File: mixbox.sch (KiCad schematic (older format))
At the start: 20 parts, among them J1 Conn_01x05_Male, J2 Conn_01x06_Male, SW1 SW_Push, SW2 SW_Push, SW3 SW_Push, SW4 SW_Push, SW5 SW_Push, SW6 SW_Push, SW7 SW_Push, SW8 SW_Push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

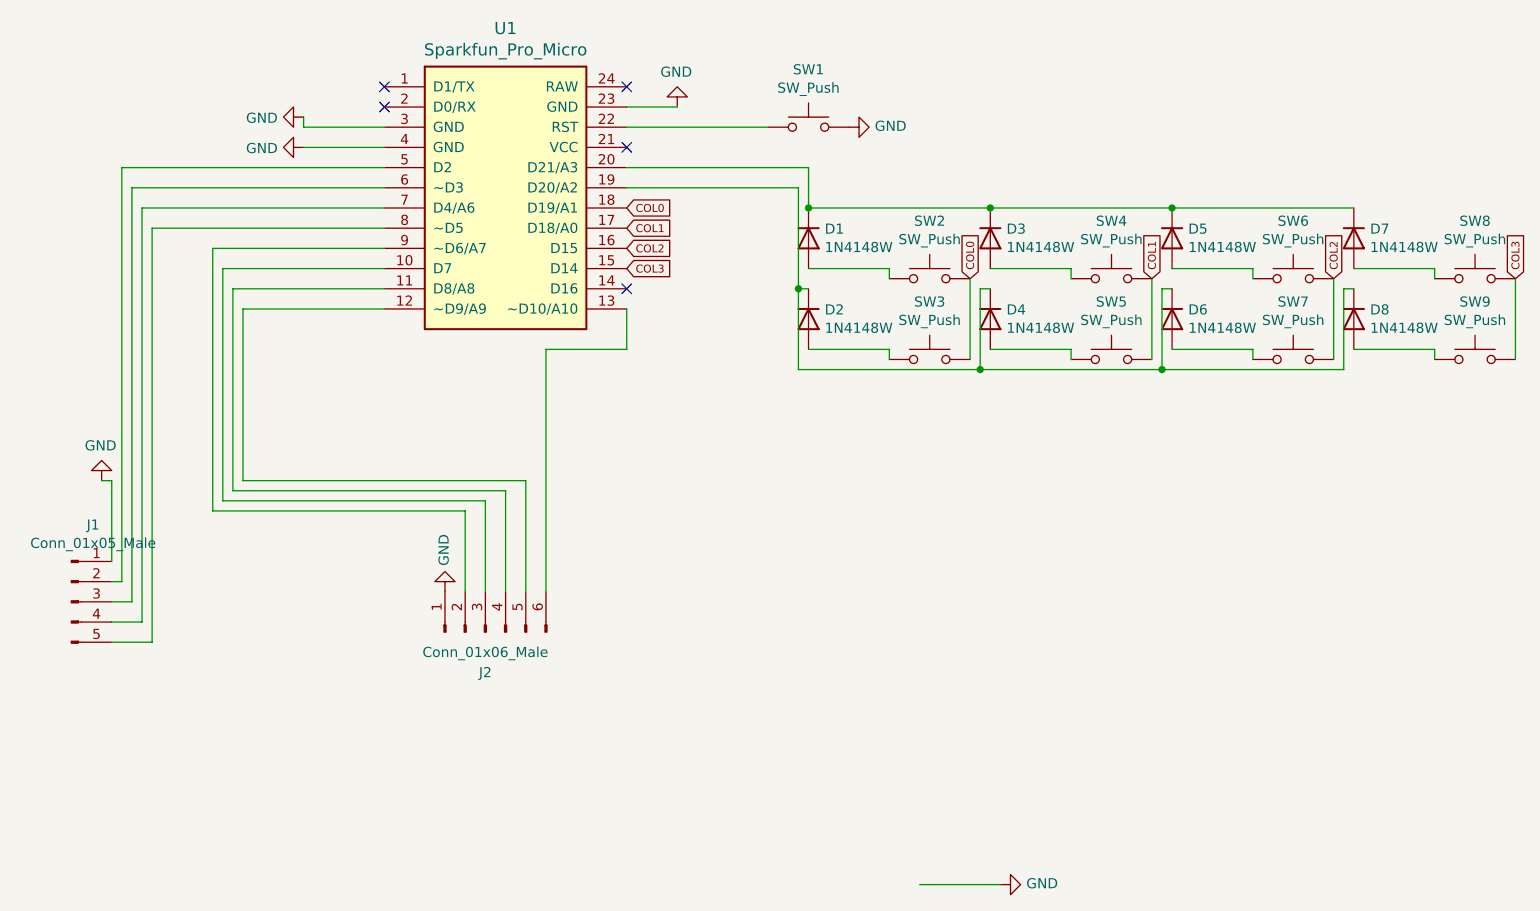
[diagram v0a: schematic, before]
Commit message: Updates schematic for 2 extra rows and columns from direct pin from the J1 and J2 connectors
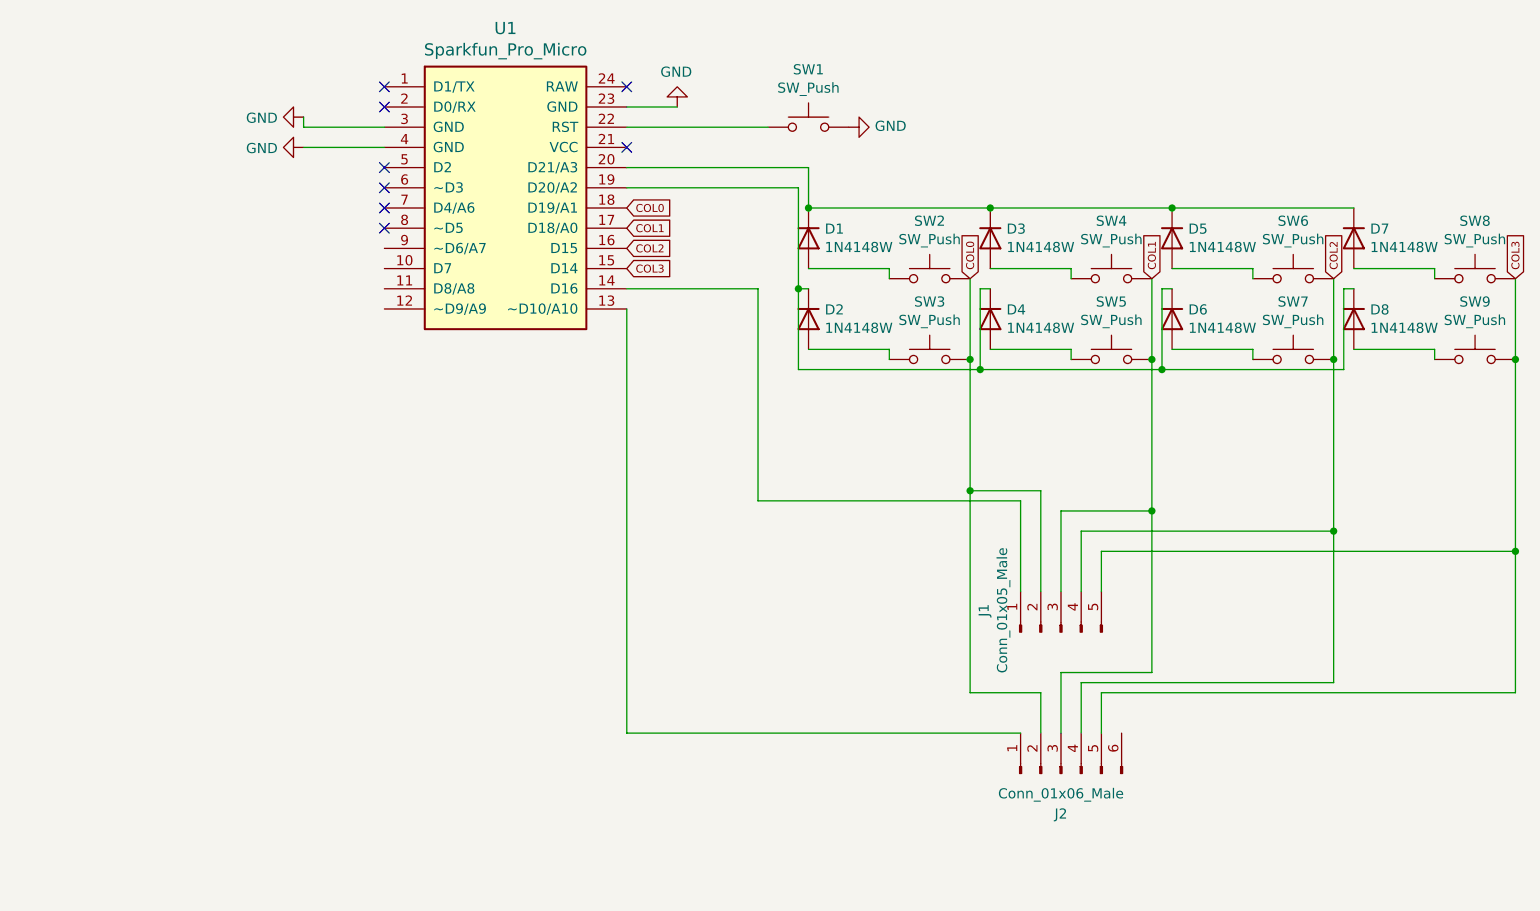
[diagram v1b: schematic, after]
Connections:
- net COL0: now also J1.2 (Pin_2), J2.2 (Pin_2)
- net COL1: now also J1.3 (Pin_3), J2.3 (Pin_3)
- net COL2: now also J1.4 (Pin_4), J2.4 (Pin_4)
- net COL3: now also J1.5 (Pin_5), J2.5 (Pin_5)
- net GND: no longer J1.1 (Pin_1), J2.1 (Pin_1)
- net at U1.9 (~~D6/A7): no longer J2.2 (Pin_2)
- net at U1.10 (D7): no longer J2.3 (Pin_3)
- net at U1.11 (D8/A8): no longer J2.4 (Pin_4)
- net at U1.12 (~~D9/A9): no longer J2.5 (Pin_5)
- net at U1.13 (~~D10/A10): now also J2.1 (Pin_1); no longer J2.6 (Pin_6)
- net at U1.14 (D16): now also J1.1 (Pin_1)
- net at U1.5 (D2): no longer J1.2 (Pin_2)
- net at U1.6 (~~D3): no longer J1.3 (Pin_3)
- net at U1.7 (D4/A6): no longer J1.4 (Pin_4)
- net at U1.8 (~~D5): no longer J1.5 (Pin_5)
- no-connect marks 5 -> 8
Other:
- moved on the sheet: J1, J2
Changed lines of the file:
@@
 $EndComp
-$Comp
-L power:GND #PWR03
-U 1 1 61D25670
-P 5300 5000
-F 0 "#PWR03" H 5300 4750 50  0001 C CNN
-F 1 "GND" V 5305 4872 50  0000 R CNN
-F 2 "" H 5300 5000 50  0001 C CNN
-F 3 "" H 5300 5000 50  0001 C CNN
-	1    5300 5000
-	0    -1   -1   0
-$EndComp
-Wire Wire Line
-	4900 5000 5300 5000
 $Comp
 L Switch:SW_Push SW1
@@
 $EndComp
 Wire Wire Line
-	4350 1950 4750 1950
-Wire Wire Line
 	4750 1950 4750 2000
 Wire Wire Line
@@
 	5200 2450 4300 2450
 Wire Wire Line
-	4300 2450 4300 2050
-Wire Wire Line
 	4300 2050 4350 2050
 Connection ~ 5200 2450
@@
 	4300 1550 3450 1550
 Connection ~ 4300 2050
-$Comp
-L Connector:Conn_01x05_Male J1
-U 1 1 61D20DF3
-P 700 3600
-F 0 "J1" H 808 3981 50  0000 C CNN
-F 1 "Conn_01x05_Male" H 808 3890 50  0000 C CNN
-F 2 "Connector_JST:JST_PH_S5B-PH-K_1x05_P2.00mm_Horizontal" H 700 3600 50  0001 C CNN
-F 3 "~" H 700 3600 50  0001 C CNN
-	1    700  3600
-	1    0    0    -1
-$EndComp
-Wire Wire Line
-	900  3500 950  3500
-Wire Wire Line
-	900  3600 1000 3600
-Wire Wire Line
-	900  3700 1050 3700
-$Comp
-L power:GND #PWR01
-U 1 1 61DB55A5
-P 850 3000
-F 0 "#PWR01" H 850 2750 50  0001 C CNN
-F 1 "GND" H 855 2827 50  0000 C CNN
-F 2 "" H 850 3000 50  0001 C CNN
-F 3 "" H 850 3000 50  0001 C CNN
-	1    850  3000
-	-1   0    0    1
-$EndComp
 $Comp
 L power:GND #PWR0101
@@
 Text GLabel 3450 1950 2    39   Input ~ 0
 COL3
-NoConn ~ 3450 2050
 NoConn ~ 3450 1350
 NoConn ~ 3450 1050
@@
 Wire Wire Line
 	1850 1250 1850 1200
-Wire Wire Line
-	900  3400 900  3000
-Wire Wire Line
-	900  3000 850  3000
-Wire Wire Line
-	950  1450 2250 1450
-Wire Wire Line
-	950  1450 950  3500
-Wire Wire Line
-	1000 1550 2250 1550
-Wire Wire Line
-	1000 1550 1000 3600
-Wire Wire Line
-	1050 1650 2250 1650
-Wire Wire Line
-	1050 1650 1050 3700
-Wire Wire Line
-	900  3800 1100 3800
-Wire Wire Line
-	1100 3800 1100 1750
-Wire Wire Line
-	1100 1750 2250 1750
 $Comp
 L Connector:Conn_01x06_Male J2
 U 1 1 61CFB837
-P 2750 3750
-F 0 "J2" V 2550 3750 50  0000 C CNN
-F 1 "Conn_01x06_Male" V 2650 3750 50  0000 C CNN
-F 2 "Connector_JST:JST_PH_S6B-PH-K_1x06_P2.00mm_Horizontal" H 2750 3750 50  0001 C CNN
-F 3 "~" H 2750 3750 50  0001 C CNN
-	1    2750 3750
+P 5600 4450
+F 0 "J2" V 5400 4450 50  0000 C CNN
+F 1 "Conn_01x06_Male" V 5500 4450 50  0000 C CNN
+F 2 "Connector_JST:JST_PH_S6B-PH-K_1x06_P2.00mm_Horizontal" H 5600 4450 50  0001 C CNN
+F 3 "~" H 5600 4450 50  0001 C CNN
+	1    5600 4450
 	0    -1   -1   0
 $EndComp
-$Comp
-L power:GND #PWR0104
-U 1 1 61D007FD
-P 2550 3550
-F 0 "#PWR0104" H 2550 3300 50  0001 C CNN
-F 1 "GND" V 2555 3422 50  0000 R CNN
-F 2 "" H 2550 3550 50  0001 C CNN
-F 3 "" H 2550 3550 50  0001 C CNN
-	1    2550 3550
-	-1   0    0    1
-$EndComp
-Wire Wire Line
-	2650 3550 2650 3150
-Wire Wire Line
-	2650 3150 1400 3150
-Wire Wire Line
-	1400 3150 1400 1850
-Wire Wire Line
-	1400 1850 2250 1850
-Wire Wire Line
-	2750 3550 2750 3100
-Wire Wire Line
-	2750 3100 1450 3100
-Wire Wire Line
-	1450 3100 1450 1950
-Wire Wire Line
-	1450 1950 2250 1950
-Wire Wire Line
-	2850 3550 2850 3050
-Wire Wire Line
-	2850 3050 1500 3050
-Wire Wire Line
-	1500 3050 1500 2050
-Wire Wire Line
-	1500 2050 2250 2050
-Wire Wire Line
-	2950 3550 2950 3000
-Wire Wire Line
-	2950 3000 1550 3000
-Wire Wire Line
-	1550 3000 1550 2150
-Wire Wire Line
-	1550 2150 2250 2150
-Wire Wire Line
-	3050 3550 3050 2350
-Wire Wire Line
-	3050 2350 3450 2350
-Wire Wire Line
-	3450 2350 3450 2150
+Wire Wire Line
+	4350 1950 4750 1950
+Wire Wire Line
+	5800 3550 5800 3350
+$Comp
+L Connector:Conn_01x05_Male J1
+U 1 1 61D20DF3
+P 5600 3750
+F 0 "J1" H 5708 4131 50  0000 C CNN
+F 1 "Conn_01x05_Male" H 5708 4040 50  0000 C CNN
+F 2 "Connector_JST:JST_PH_S5B-PH-K_1x05_P2.00mm_Horizontal" H 5600 3750 50  0001 C CNN
+F 3 "~" H 5600 3750 50  0001 C CNN
+	1    5600 3750
+	0    -1   -1   0
+$EndComp
+Wire Wire Line
+	4300 2450 4300 2050
+Wire Wire Line
+	5800 3350 7850 3350
+Wire Wire Line
+	7850 3350 7850 2400
+Connection ~ 7850 2400
+Wire Wire Line
+	5700 3250 6950 3250
+Wire Wire Line
+	6950 3250 6950 2400
+Wire Wire Line
+	5700 3250 5700 3550
+Connection ~ 6950 2400
+Wire Wire Line
+	5600 3150 6050 3150
+Wire Wire Line
+	6050 3150 6050 2400
+Wire Wire Line
+	5600 3150 5600 3550
+Connection ~ 6050 2400
+Wire Wire Line
+	5500 3050 5150 3050
+Wire Wire Line
+	5150 3050 5150 2400
+Wire Wire Line
+	5500 3050 5500 3550
+Connection ~ 5150 2400
+Wire Wire Line
+	5400 3550 5400 3100
+Wire Wire Line
+	5400 3100 4100 3100
+Wire Wire Line
+	4100 3100 4100 2050
+Wire Wire Line
+	4100 2050 3450 2050
+NoConn ~ 2250 1450
+NoConn ~ 2250 1550
+NoConn ~ 2250 1650
+NoConn ~ 2250 1750
+Wire Wire Line
+	5800 4250 5800 4050
+Wire Wire Line
+	5800 4050 7850 4050
+Wire Wire Line
+	7850 4050 7850 3350
+Connection ~ 7850 3350
+Wire Wire Line
+	5700 4250 5700 4000
+Wire Wire Line
+	5700 4000 6950 4000
+Wire Wire Line
+	6950 4000 6950 3250
+Connection ~ 6950 3250
+Wire Wire Line
+	5600 4250 5600 3950
+Wire Wire Line
+	5600 3950 6050 3950
+Wire Wire Line
+	6050 3950 6050 3150
+Connection ~ 6050 3150
+Wire Wire Line
+	5500 4250 5500 4050
+Wire Wire Line
+	5500 4050 5150 4050
+Wire Wire Line
+	5150 4050 5150 3050
+Connection ~ 5150 3050
+Wire Wire Line
+	5400 4250 3450 4250
+Wire Wire Line
+	3450 4250 3450 2150
 $EndSCHEMATC

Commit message: Updates rows and columns in pcbnew and updates J2 from 1x06 to 1x05 connector
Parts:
- J2: value Conn_01x06_Male -> Conn_01x05_Male; footprint Connector_JST:JST_PH_S6B-PH-K_1x06_P2.00mm_Horizontal -> Connector_JST:JST_PH_S5B-PH-K_1x05_P2.00mm_Horizontal; symbol Connector:Conn_01x06_Male -> Connector:Conn_01x05_Male
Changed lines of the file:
@@
 COL3
 NoConn ~ 3450 1350
-NoConn ~ 3450 1050
 NoConn ~ 2250 1150
 NoConn ~ 2250 1050
@@
 $EndComp
 Wire Wire Line
-	2250 1350 1850 1350
-Wire Wire Line
-	2250 1250 1850 1250
-Wire Wire Line
 	1850 1250 1850 1200
 $Comp
-L Connector:Conn_01x06_Male J2
+L Connector:Conn_01x05_Male J2
 U 1 1 61CFB837
 P 5600 4450
 F 0 "J2" V 5400 4450 50  0000 C CNN
-F 1 "Conn_01x06_Male" V 5500 4450 50  0000 C CNN
-F 2 "Connector_JST:JST_PH_S6B-PH-K_1x06_P2.00mm_Horizontal" H 5600 4450 50  0001 C CNN
+F 1 "Conn_01x05_Male" V 5500 4450 50  0000 C CNN
+F 2 "Connector_JST:JST_PH_S5B-PH-K_1x05_P2.00mm_Horizontal" H 5600 4450 50  0001 C CNN
 F 3 "~" H 5600 4450 50  0001 C CNN
 	1    5600 4450
@@
 Wire Wire Line
 	3450 4250 3450 2150
+Wire Wire Line
+	2250 1350 1850 1350
+Wire Wire Line
+	2250 1250 1850 1250
+NoConn ~ 3450 1050
 $EndSCHEMATC

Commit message: Adds pwr_flag to schematic gnd
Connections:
- no-connect marks 8 -> 12
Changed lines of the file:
@@
 	3450 1250 4150 1250
 Wire Wire Line
-	3450 1150 3700 1150
+	3450 1150 3550 1150
 Text GLabel 5150 2000 1    39   Input ~ 0
 COL0
@@
 NoConn ~ 2250 1150
 NoConn ~ 2250 1050
-$Comp
-L power:GND #PWR0102
-U 1 1 61E04168
-P 1850 1200
-F 0 "#PWR0102" H 1850 950 50  0001 C CNN
-F 1 "GND" V 1855 1072 50  0000 R CNN
-F 2 "" H 1850 1200 50  0001 C CNN
-F 3 "" H 1850 1200 50  0001 C CNN
-	1    1850 1200
-	0    1    1    0
-$EndComp
-$Comp
-L power:GND #PWR0103
-U 1 1 61E053F4
-P 1850 1350
-F 0 "#PWR0103" H 1850 1100 50  0001 C CNN
-F 1 "GND" V 1855 1222 50  0000 R CNN
-F 2 "" H 1850 1350 50  0001 C CNN
-F 3 "" H 1850 1350 50  0001 C CNN
-	1    1850 1350
-	0    1    1    0
-$EndComp
 Wire Wire Line
 	1850 1250 1850 1200
@@
 	3450 4250 3450 2150
 Wire Wire Line
-	2250 1350 1850 1350
+	2250 1350 2000 1350
 Wire Wire Line
-	2250 1250 1850 1250
+	2250 1250 2000 1250
 NoConn ~ 3450 1050
+Wire Wire Line
+	2000 1350 2000 1250
+Connection ~ 2000 1250
+Wire Wire Line
+	2000 1250 1850 1250
+Wire Wire Line
+	2000 1250 2000 700
+Wire Wire Line
+	2000 700  3550 700
+Wire Wire Line
+	3550 700  3550 800
+Connection ~ 3550 1150
+Wire Wire Line
+	3550 1150 3700 1150
+Wire Wire Line
+	4550 1250 4550 800
+Wire Wire Line
+	4550 800  3550 800
+Connection ~ 4550 1250
+Connection ~ 3550 800
+Wire Wire Line
+	3550 800  3550 1150
+NoConn ~ 2250 1850
+NoConn ~ 2250 1950
+NoConn ~ 2250 2050
+NoConn ~ 2250 2150
+$Comp
+L power:PWR_FLAG #FLG0101
+U 1 1 61DC0042
+P 1850 1200
+F 0 "#FLG0101" H 1850 1275 50  0001 C CNN
+F 1 "PWR_FLAG" H 1850 1373 50  0000 C CNN
+F 2 "" H 1850 1200 50  0001 C CNN
+F 3 "~" H 1850 1200 50  0001 C CNN
+	1    1850 1200
+	1    0    0    -1
+$EndComp
 $EndSCHEMATC
